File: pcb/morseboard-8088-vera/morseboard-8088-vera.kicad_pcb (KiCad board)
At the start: 2 copper layers, 174.4 x 127 mm, 62 parts, among them J1 USB_B, J2 UART1, J3 Bus, SW1 SW_SPDT, SW2 INTPORT, SW4 NMI, SW6 RESET, U1 8088, U10 74HCT273, U11 TL16C550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

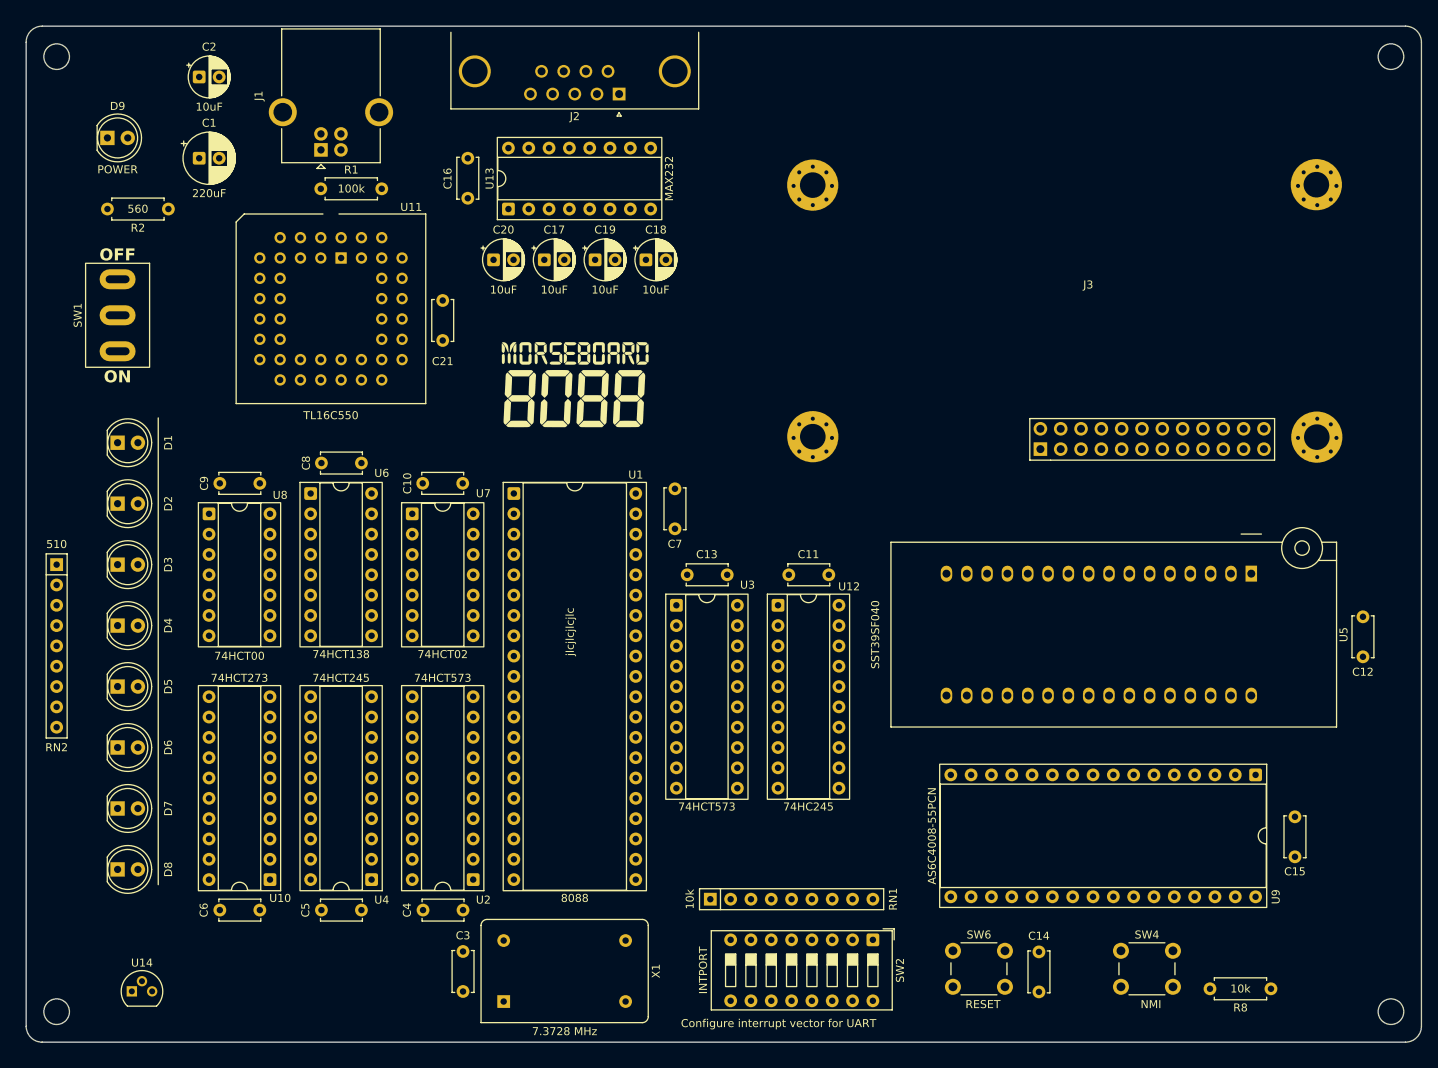
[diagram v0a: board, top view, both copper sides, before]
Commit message: Further shaping board
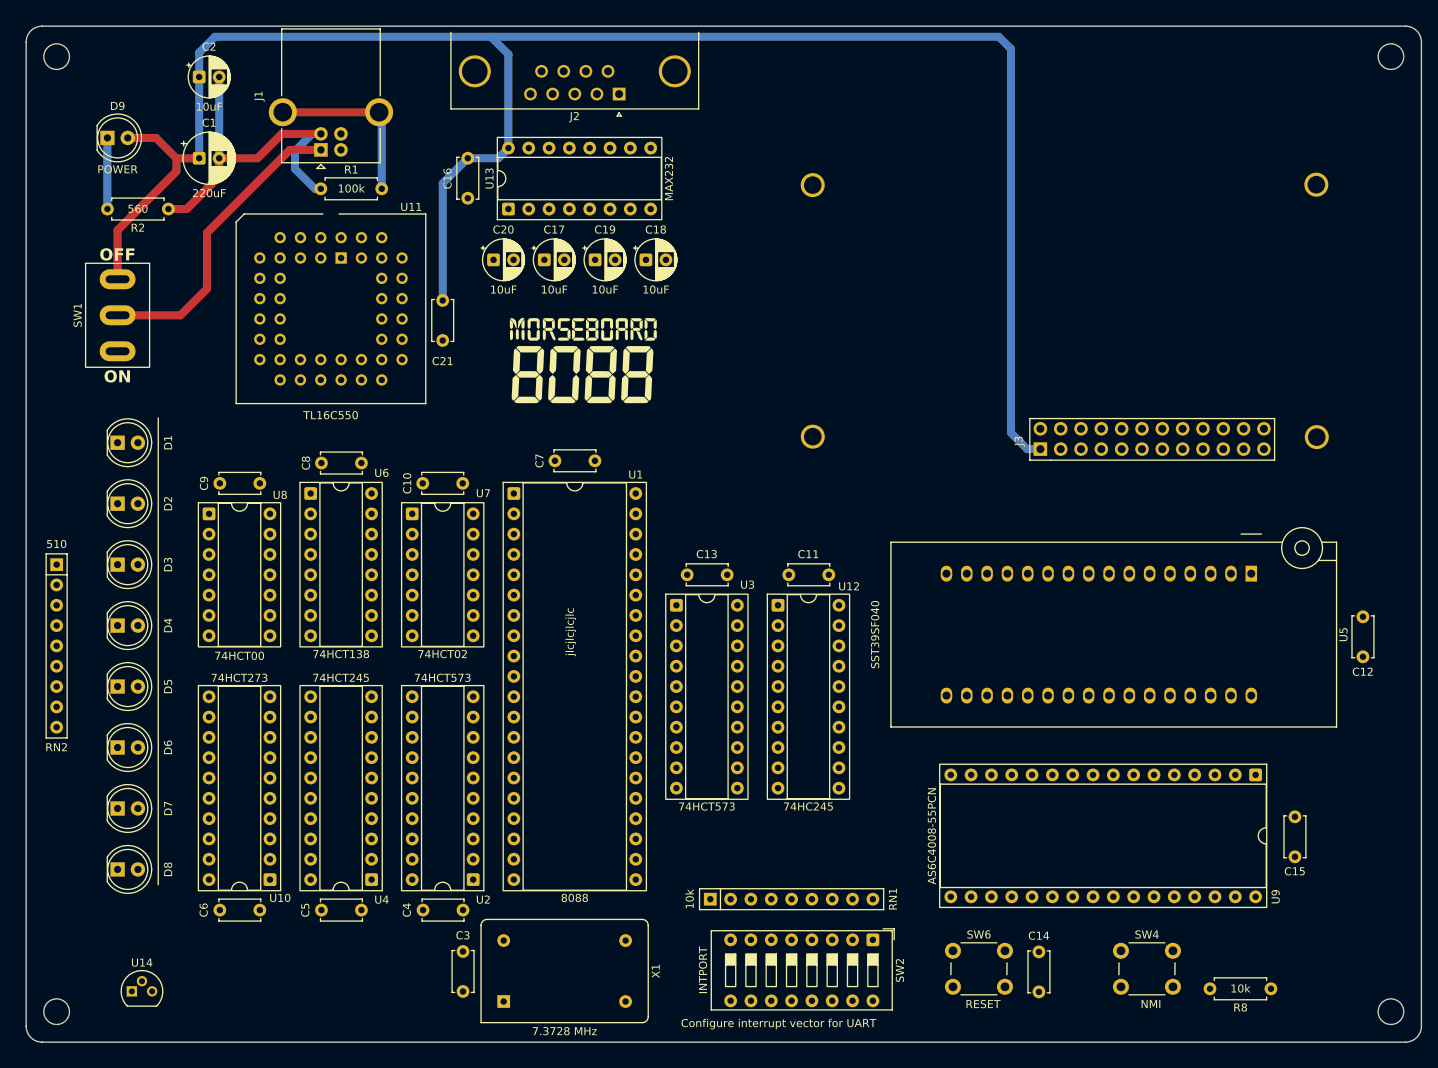
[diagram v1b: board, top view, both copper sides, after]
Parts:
- moved C7 10.6 mm to (96.5, 81.0), turned to 180 degrees
- moved G001 3.17 mm to (95.0, 68.5)
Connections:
- J3 pad 22: unconnected-(J3-Pin_22-Pad22) -> GND
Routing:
- net VCC: track 0.00 -> 236.3 mm
- net GND: track 0.00 -> 45.1 mm
- net VIN: track 0.00 -> 38.1 mm
- net Net-(J1-Shield): track 0.00 -> 21.7 mm
- net Net-(D9-K): track 0.00 -> 8.89 mm

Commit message: Further drawing traces
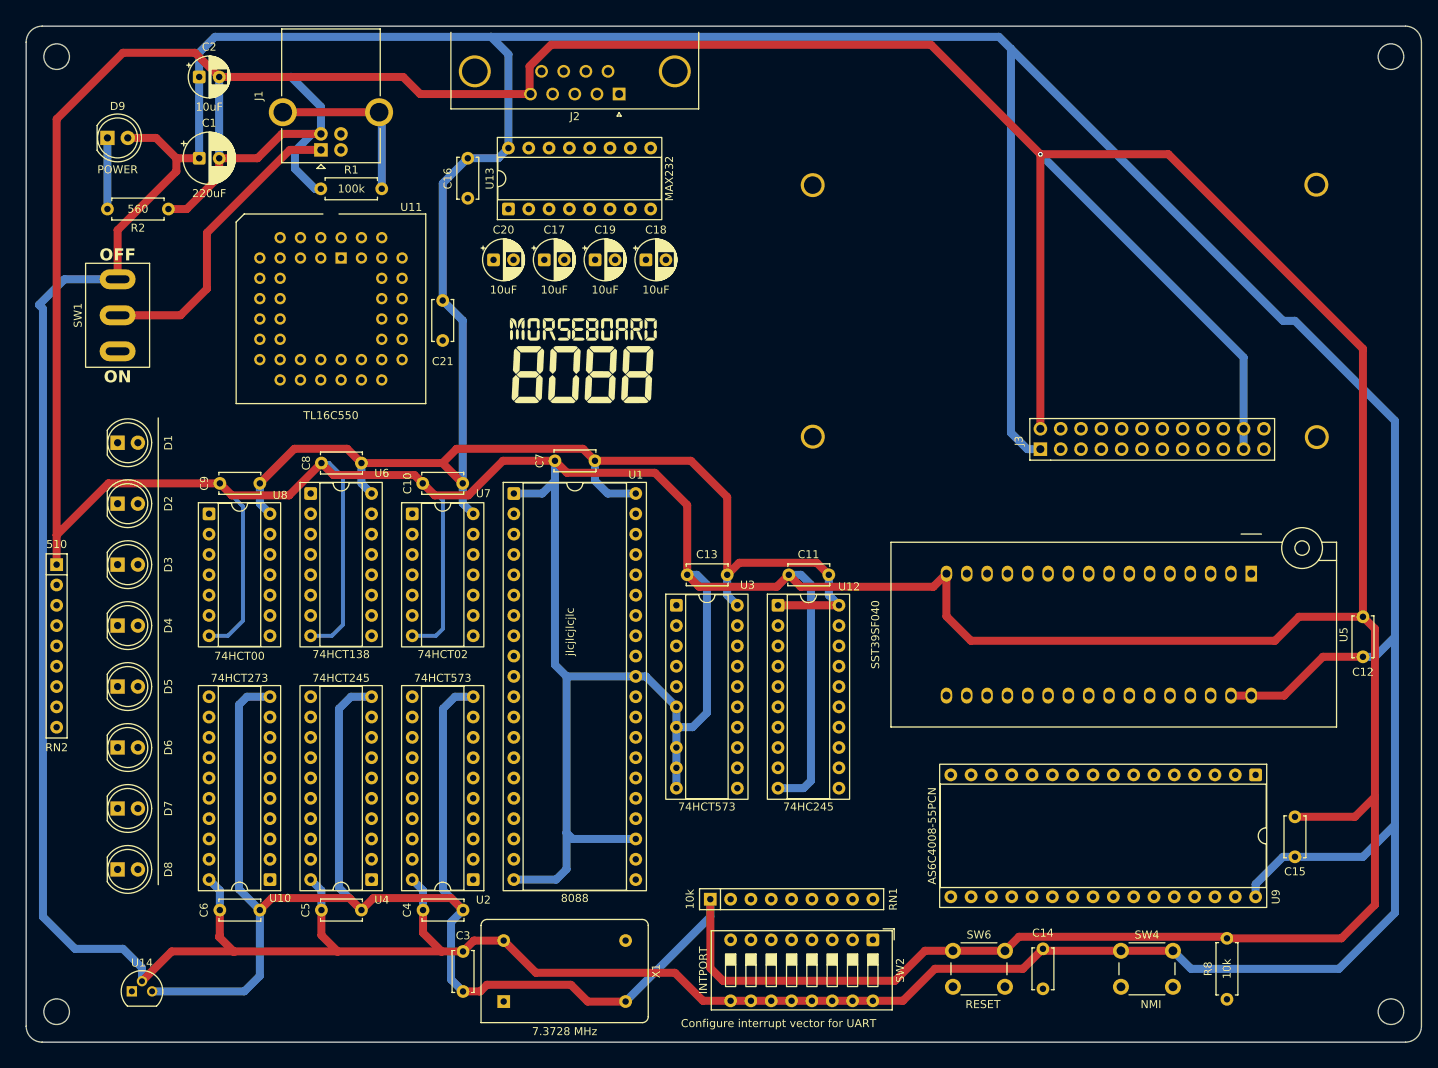
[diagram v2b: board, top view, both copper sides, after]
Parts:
- moved R8 5.65 mm to (175.5, 148.3), turned to 90 degrees
- moved C14 0.63 mm to (152.5, 147.0)
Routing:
- net GND: track 45.1 -> 1181.8 mm, vias 0 -> 1
- net VCC: track 236.3 -> 868.0 mm

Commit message: Routing VERA prototype
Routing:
- net D7: track 0.00 -> 296.1 mm, vias 0 -> 1
- net D6: track 0.00 -> 291.1 mm, vias 0 -> 2
- net D4: track 0.00 -> 285.7 mm, vias 0 -> 1
- net D5: track 0.00 -> 280.9 mm, vias 0 -> 1
- net ~{RES}: track 0.00 -> 267.1 mm
- net D2: track 0.00 -> 258.9 mm, vias 0 -> 1
- net D0: track 0.00 -> 254.6 mm, vias 0 -> 3
- net D1: track 0.00 -> 252.2 mm, vias 0 -> 2
- net D3: track 0.00 -> 251.4 mm, vias 0 -> 2
- net A0: track 0.00 -> 223.9 mm
- net ~{WR}: track 0.00 -> 219.2 mm, vias 0 -> 2
- net A1: track 0.00 -> 213.7 mm, vias 0 -> 1
- net A2: track 0.00 -> 197.8 mm, vias 0 -> 2
- net ~{RD}: track 0.00 -> 186.5 mm, vias 0 -> 1
- net A6: track 0.00 -> 172.4 mm, vias 0 -> 2
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- added copper zone on F.Cu, net GND
- added copper zone on B.Cu, net VCC

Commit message: Building VERA prototype
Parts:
- removed RN1: 10k, Resistor_THT:R_Array_SIP9
- removed SW2: INTPORT, Button_Switch_THT:SW_DIP_SPSTx08_Slide_9.78x22.5mm_W7.62mm_P2.54mm
- added C22: 22pF, Capacitor_THT:C_Disc_D5.0mm_W2.5mm_P5.00mm, F.Cu at (156.7, 50.8)
- added C23: 22pF, Capacitor_THT:C_Disc_D5.0mm_W2.5mm_P5.00mm, F.Cu at (151.8, 68.6)
- added C24: 100nF, Capacitor_THT:C_Disc_D5.0mm_W2.5mm_P5.00mm, F.Cu at (161.8, 33.0)
- added C25: 100nF, Capacitor_THT:C_Disc_D5.0mm_W2.5mm_P5.00mm, F.Cu at (116.8, 149.9)
- added C26: 100nF, Capacitor_THT:C_Disc_D5.0mm_W2.5mm_P5.00mm, F.Cu at (138.4, 149.9)
- added C27: 100nF, Capacitor_THT:C_Disc_D5.0mm_W2.5mm_P5.00mm, F.Cu at (172.6, 55.8)
- added J4: Mini-DIN-6, components:J_Mini-DIN-6, F.Cu at (64.8, 26.9)
- added J5: Conn_01x03_Pin, Connector_PinHeader_2.54mm:PinHeader_1x03_P2.54mm_Vertical, F.Cu at (184.8, 48.8)
- added R10: 10k, Resistor_THT:R_Axial_DIN0207_L6.3mm_D2.5mm_P7.62mm_Horizontal, F.Cu at (152.4, 149.9)
- added R11: 10k, Resistor_THT:R_Axial_DIN0207_L6.3mm_D2.5mm_P7.62mm_Horizontal, F.Cu at (156.8, 72.4)
- added R3: 10k, Resistor_THT:R_Axial_DIN0207_L6.3mm_D2.5mm_P7.62mm_Horizontal, F.Cu at (154.2, 38.1)
- added R9: 10k, Resistor_THT:R_Axial_DIN0207_L6.3mm_D2.5mm_P7.62mm_Horizontal, F.Cu at (130.8, 149.9)
- added SW5: ON, Button_Switch_THT:SW_PUSH_6mm, F.Cu at (120.7, 145.4)
- added Y1: Crystal, Crystal:Crystal_HC49-4H_Vertical, F.Cu at (154.2, 62.1)
- U12: value 74HC245 -> ATmega328P-P; footprint Package_DIP:DIP-20_W7.62mm_Socket -> Package_DIP:DIP-28_W7.62mm_Socket
- U14: value DS1813 -> 74HCT245; footprint Package_TO_SOT_THT:TO-92 -> Package_DIP:DIP-20_W7.62mm_Socket
- U5: footprint Socket:DIP_Socket-32_W11.9_W12.7_W15.24_W17.78_W18.5_3M_232-1285-00-0602J -> Socket:DIP_Socket-32_W11.9mm_W12.7mm_W15.24mm_W17.78mm_W18.5mm_3M_232-1285-00-0602J
- moved U14 143.5 mm to (137.2, 43.0)
- moved D9 109.7 mm to (63.5, 146.7)
- moved R2 102.2 mm to (59.1, 150.5), turned to 90 degrees
- moved U12 73.6 mm to (160.6, 38.1)
- moved C11 59.4 mm to (143.5, 38.6)
- moved C13 58.6 mm to (128.2, 38.6)
- moved U3 58.0 mm to (121.9, 43.0)
- moved C2 22.2 mm to (33.7, 50.8)
- moved U9 21.7 mm to (157.4, 120.8)
- moved C12 21.7 mm to (170.8, 106.0)
- moved C15 21.7 mm to (162.3, 131.0)
- moved U5 21.7 mm to (156.8, 95.6)
- moved J1 20.3 mm to (41.9, 42.8)
- moved C1 9.16 mm to (42.0, 50.8)
- moved H2 8.68 mm to (187.3, 30.5)
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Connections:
- J3 pad 14: unconnected-(J3-Pin_14-Pad14) -> VERA_INT
- SW6 pad 1: GND -> VCC
- SW6 pad 2: ~{RES} -> RESET_BTN
- U11 pad 33: INTR -> SERIAL_INT
- U12 pad 1: VCC -> Net-(U12-~{RESET}/PC6)
- U12 pad 10: GND -> Net-(U12-XTAL2/PB7)
- U12 pad 11: D7 -> CD5
- U12 pad 12: D6 -> CD6
- U12 pad 13: D5 -> CD7
- U12 pad 14: D4 -> ~{RES}
- U12 pad 15: D3 -> INTR
- U12 pad 16: D2 -> ~{INTA}
- U12 pad 17: D1 -> VERA_INT
- U12 pad 18: D0 -> ~{IO03}
- U12 pad 19: ~{INTA} -> KB_DATA
- U12 pad 2: Net-(RN1-R8) -> CTRL_RXD
- U12 pad 3: Net-(RN1-R7) -> CTRL_TXD
- U12 pad 4: Net-(RN1-R6) -> KB_CLK
- U12 pad 5: Net-(RN1-R5) -> SERIAL_INT
- U12 pad 6: Net-(RN1-R4) -> CD4
- U12 pad 7: Net-(RN1-R3) -> VCC
- U12 pad 8: Net-(RN1-R2) -> GND
- U14 pad 1: ~{RES} -> VCC
- U14 pad 2: VCC -> CD0
- U14 pad 3: GND -> CD1
- U6 pad 12: unconnected-(U6-~{Y3}-Pad12) -> ~{IO03}
- U7 pad 10: unconnected-(U7-Pad10) -> Net-(U7-Pad10)
- U7 pad 11: VCC -> Net-(U7-Pad10)
- U7 pad 12: VCC -> Net-(U7-Pad10)
- U7 pad 13: unconnected-(U7-Pad13) -> Net-(U14-CE)
- U7 pad 8: VCC -> ~{INTA}
- U7 pad 9: VCC -> ~{IO03}
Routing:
- net GND: track 1309.5 -> 1539.1 mm, vias 1 -> 0
- net VCC: track 982.1 -> 1161.6 mm
- net ON_BTN: track 0.00 -> 151.6 mm
- net RESET_BTN: track 0.00 -> 137.2 mm
- net KB_DATA: track 0.00 -> 133.1 mm, vias 0 -> 1
- net ~{IO03}: track 0.00 -> 119.3 mm, vias 0 -> 1
- net KB_CLK: track 0.00 -> 115.4 mm
- net AD0: track 23.3 -> 137.1 mm
- net AD1: track 26.5 -> 139.6 mm, vias 2 -> 1
- net ~{RES}: track 267.1 -> 160.1 mm, vias 0 -> 1
- net AD3: track 24.7 -> 129.7 mm
- net AD7: track 24.9 -> 125.3 mm
- net AD5: track 24.9 -> 124.4 mm
- net AD6: track 23.9 -> 121.1 mm
- net AD2: track 26.7 -> 123.3 mm, vias 1 -> 2
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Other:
- board size 174.4 x 127 mm -> 165.7 x 127 mm
- board text added: "GND"
- board text added: "RXD"
- board text added: "TXD"
- board text added: "VERA"
- board text removed: "Configure interrupt vector for UART"
